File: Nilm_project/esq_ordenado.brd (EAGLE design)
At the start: 115.5 x 100 mm, 37 parts, among them IC1 LM1117IMPX-3.3, J4 10103594-0001LF, Q1 SMD-TRANSISTORS-NPN-25V-500MW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, Q2 SMD-TRANSISTORS-NPN-25V-500MW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, U1 ESP-32S, U2 CP2102-GM, U3 TPD2S017DBVR, U4 SP0503BAHT

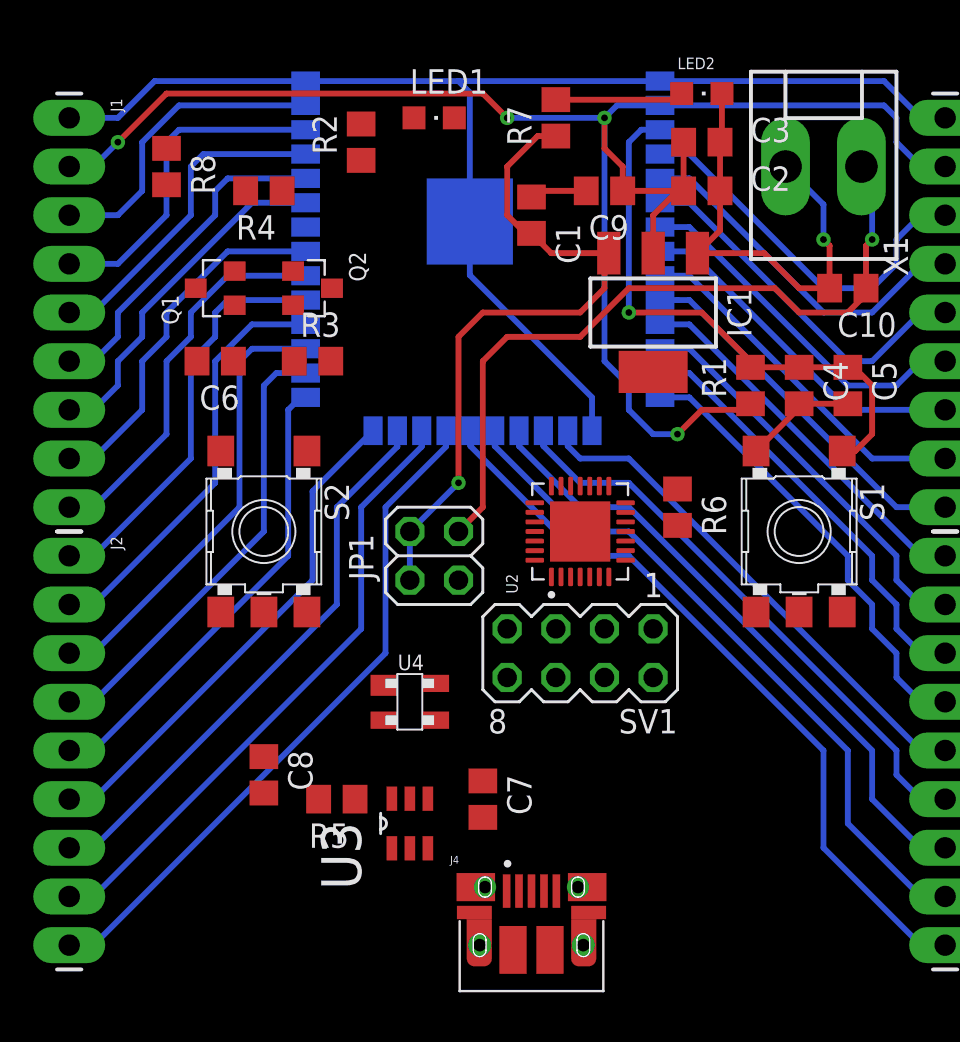
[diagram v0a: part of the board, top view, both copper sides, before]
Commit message: Adicionando Datasheet TPD2S017 y conexiones entre D+ y D- a la regleta
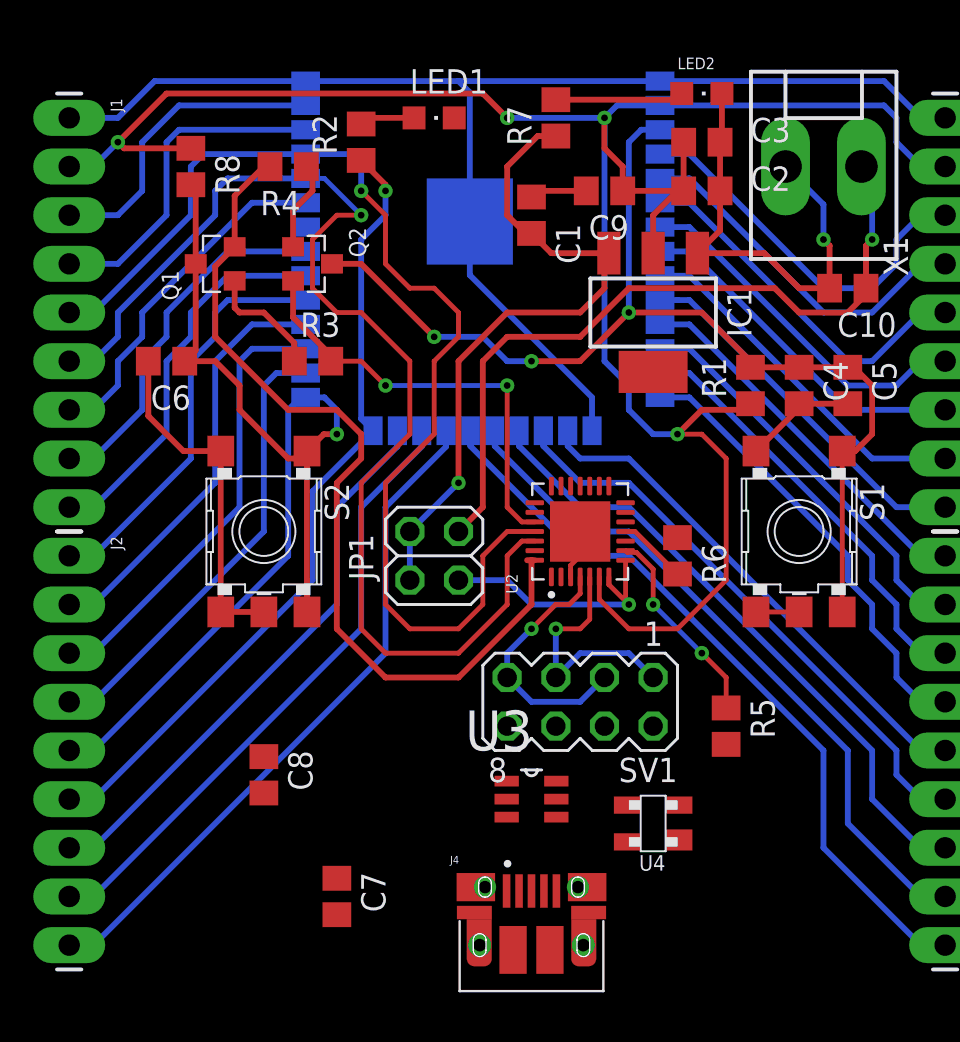
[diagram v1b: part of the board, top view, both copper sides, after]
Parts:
- moved R5 20.7 mm to (92.7, 55.9), turned to 90 degrees
- moved U4 14.2 mm to (88.9, 50.8), turned to 180 degrees
- moved C7 9.16 mm to (72.4, 47.0)
- moved U3 6.48 mm to (82.5, 52.1), turned to 0 degrees
- moved C6 2.54 mm to (63.5, 74.9)
- moved R6 2.54 mm to (90.2, 64.8)
- moved SV1 2.54 mm to (85.1, 57.1)
- moved R4 1.80 mm to (69.8, 85.1)
- moved Q1 1.27 mm to (66.0, 80.0)
- moved Q2 1.27 mm to (71.1, 80.0)
- moved R8 1.27 mm to (64.8, 85.1)
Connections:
- removed net D+_IN: SV1.6, U3.1
- removed net D-_IN: SV1.8, U3.6
- new net D+IN: SV1.8, U3.1
- new net D-IN: SV1.6, U3.6
- net D+: now also SV1.3, SV1.7; no longer SV1.1, SV1.5
- net D+_OUT: now also SV1.4; no longer SV1.2
- net D-: now also SV1.1, SV1.5; no longer SV1.3, SV1.7
- net D-_OUT: now also SV1.2; no longer SV1.4
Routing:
- net DTR_CP: track 0.00 -> 46.6 mm
- net RXD_ESP: track 17.8 -> 62.3 mm, vias 0 -> 1
- net TXD_ESP: track 17.3 -> 59.6 mm, vias 0 -> 1
- net IO0: track 24.4 -> 56.9 mm, vias 0 -> 1
- net ENABLE: track 30.3 -> 57.4 mm, vias 1 -> 3
- net 3.3V: track 87.7 -> 111.0 mm
- net GND: track 101.8 -> 124.6 mm
- net RTS_CP: track 0.00 -> 22.9 mm, vias 0 -> 2
- net IO2: track 26.5 -> 42.0 mm, vias 0 -> 1
- net VUSB: track 0.00 -> 13.7 mm, vias 0 -> 1
- net D+: track 0.00 -> 13.4 mm, vias 0 -> 1
- net D-: track 0.00 -> 12.9 mm, vias 0 -> 1
- net N$5: track 0.00 -> 10.7 mm, vias 0 -> 2
- net N$3: track 0.00 -> 6.22 mm
- net N$4: track 0.00 -> 4.74 mm
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
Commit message: Correcciones D+ Y D- en TPD2S017 y en los pines, para un mejor ruteo
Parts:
- moved C7 7.18 mm to (67.3, 52.1), turned to 0 degrees
- moved C8 2.84 mm to (67.3, 55.9), turned to 0 degrees
- moved U3 1.27 mm to (81.3, 52.1), flipped to the bottom
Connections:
- net D+: now also SV1.1, SV1.5; no longer SV1.3, SV1.7
- net D+IN: now also SV1.6; no longer SV1.8
- net D+_OUT: now also SV1.2; no longer SV1.4
- net D-: now also SV1.3, SV1.7; no longer SV1.1, SV1.5
- net D-IN: now also SV1.8; no longer SV1.6
- net D-_OUT: now also SV1.4; no longer SV1.2
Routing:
- net GND: track 124.6 -> 223.5 mm, vias 1 -> 7
- net VUSB: track 13.7 -> 41.9 mm, vias 1 -> 2
- net D+: track 13.4 -> 0.00 mm, vias 1 -> 0
- net D-: track 12.9 -> 0.00 mm, vias 1 -> 0

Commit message: PCB terminada cumpliendo la mayoria de normas
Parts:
- moved C7 7.41 mm to (73.7, 48.3), turned to 180 degrees
- moved C8 7.41 mm to (73.7, 52.1), turned to 180 degrees
- moved R5 1.80 mm to (94.0, 54.6)
- moved U4 1.27 mm to (87.6, 50.8), flipped to the bottom, turned to 90 degrees
- moved U3 1.27 mm to (82.5, 52.1)
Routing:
- net 3.3V: track 111.0 -> 193.5 mm, vias 4 -> 6
- net GND: track 223.5 -> 260.2 mm, vias 7 -> 10
- net VUSB: track 41.9 -> 67.7 mm
- net D-_OUT: track 0.00 -> 21.6 mm, vias 0 -> 3
- net D+_OUT: track 0.00 -> 13.6 mm, vias 0 -> 1
- net D+: track 0.00 -> 11.9 mm, vias 0 -> 1
- net D-: track 0.00 -> 11.7 mm, vias 0 -> 1
- net D-IN: track 0.00 -> 2.88 mm
- net D+IN: track 0.00 -> 2.88 mm
- net N$5: track 10.7 -> 12.5 mm
- added copper zone on layer 1, net GND
- added copper zone on layer 16, net GND
